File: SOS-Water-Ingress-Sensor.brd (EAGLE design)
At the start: 160 x 100 mm, 1 part

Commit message: Update board design and schematic.
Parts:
- added JP1: (no value), SparkFun-Connectors:1X03
- added Q1: (no value), SparkFun-DiscreteSemi:SOT23-3
- added R1, R3: 10K, resistor:R0603
- added R2: 200K, resistor:R0603
- added U$1, U$2, U$3, U$4: JSH-GH-2VERT, BlueRobotics-JST-GH:JST-GH-TOP-2
- added U$5: JST-GH-3VERT, BlueRobotics-JST-GH:JST-GH-TOP-3
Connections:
- new net GND: JP1.1, R3.2, U$1.2, U$2.2, U$3.2, U$4.2
- new net N$1: Q1.1, R1.1, R2.1
- new net PROBE: R1.2, U$1.1, U$2.1, U$3.1, U$4.1
- new net SIGNAL: JP1.3, Q1.3, R3.1
- new net VCC: JP1.2, Q1.2, R2.2
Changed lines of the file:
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@@
 <elements>
 <element name="U$7" library="BR-Eagle-Library" package="BR-LOGO-SMALL" value="LOGOBR-LOGO-S" x="-15.24" y="1.27"/>
+<element name="JP1" library="SparkFun-Connectors" package="1X03" value="" x="-13.97" y="-7.62"/>
+<element name="R2" library="resistor" package="R0603" value="200K" x="-13.97" y="-11.43"/>
+<element name="R1" library="resistor" package="R0603" value="10K" x="-19.05" y="-15.24"/>
+<element name="U$1" library="BlueRobotics-JST-GH" package="JST-GH-TOP-2" value="JSH-GH-2VERT" x="-17.78" y="-26.67"/>
+<element name="Q1" library="SparkFun-DiscreteSemi" package="SOT23-3" value="" x="-22.86" y="-29.21"/>
+<element name="R3" library="resistor" package="R0603" value="10K" x="-22.86" y="-33.02"/>
+<element name="U$2" library="BlueRobotics-JST-GH" package="JST-GH-TOP-2" value="JSH-GH-2VERT" x="-21.59" y="-36.83"/>
+<element name="U$3" library="BlueRobotics-JST-GH" package="JST-GH-TOP-2" value="JSH-GH-2VERT" x="-21.59" y="-43.18"/>
+<element name="U$4" library="BlueRobotics-JST-GH" package="JST-GH-TOP-2" value="JSH-GH-2VERT" x="-21.59" y="-49.53"/>
+<element name="U$5" library="BlueRobotics-JST-GH" package="JST-GH-TOP-3" value="JST-GH-3VERT" x="-21.59" y="-55.88"/>
 </elements>
 <signals>
+<signal name="VCC">
+<contactref element="R2" pad="2"/>
+<contactref element="Q1" pad="2"/>
+<contactref element="JP1" pad="2"/>
+<wire x1="-13.12" y1="-11.43" x2="-21.91" y2="-30.21" width="0" layer="19" extent="1-1"/>
+<wire x1="-11.43" y1="-7.62" x2="-13.12" y2="-11.43" width="0" layer="19" extent="1-1"/>
+</signal>
+<signal name="GND">
+<contactref element="JP1" pad="1"/>
+<contactref element="U$1" pad="2"/>
+<contactref element="R3" pad="2"/>
+<contactref element="U$4" pad="2"/>
+<contactref element="U$2" pad="2"/>
+<contactref element="U$3" pad="2"/>
+<wire x1="-21.59" y1="-43.18" x2="-21.59" y2="-49.53" width="0" layer="19" extent="1-1"/>
+<wire x1="-21.59" y1="-36.83" x2="-21.59" y2="-43.18" width="0" layer="19" extent="1-1"/>
+<wire x1="-22.01" y1="-33.02" x2="-21.59" y2="-36.83" width="0" layer="19" extent="1-1"/>
+<wire x1="-17.78" y1="-26.67" x2="-22.01" y2="-33.02" width="0" layer="19" extent="1-1"/>
+<wire x1="-13.97" y1="-7.62" x2="-17.78" y2="-26.67" width="0" layer="19" extent="1-1"/>
+</signal>
+<signal name="SIGNAL">
+<contactref element="JP1" pad="3"/>
+<contactref element="Q1" pad="3"/>
+<contactref element="R3" pad="1"/>
+<wire x1="-22.86" y1="-28.11" x2="-23.71" y2="-33.02" width="0" layer="19" extent="1-1"/>
+<wire x1="-8.89" y1="-7.62" x2="-22.86" y2="-28.11" width="0" layer="19" extent="1-1"/>
+</signal>
+<signal name="N$1">
+<contactref element="R1" pad="1"/>
+<contactref element="Q1" pad="1"/>
+<contactref element="R2" pad="1"/>
+<wire x1="-19.9" y1="-15.24" x2="-23.81" y2="-30.21" width="0" layer="19" extent="1-1"/>
+<wire x1="-14.82" y1="-11.43" x2="-19.9" y2="-15.24" width="0" layer="19" extent="1-1"/>
+</signal>
+<signal name="PROBE">
+<contactref element="U$1" pad="1"/>
+<contactref element="R1" pad="2"/>
+<contactref element="U$4" pad="1"/>
+<contactref element="U$2" pad="1"/>
+<contactref element="U$3" pad="1"/>
+<wire x1="-20.34" y1="-43.18" x2="-20.34" y2="-49.53" width="0" layer="19" extent="1-1"/>
+<wire x1="-20.34" y1="-36.83" x2="-20.34" y2="-43.18" width="0" layer="19" extent="1-1"/>
+<wire x1="-16.53" y1="-26.67" x2="-20.34" y2="-36.83" width="0" layer="19" extent="1-1"/>
+<wire x1="-18.2" y1="-15.24" x2="-16.53" y2="-26.67" width="0" layer="19" extent="1-1"/>
+</signal>
 </signals>
 </board>

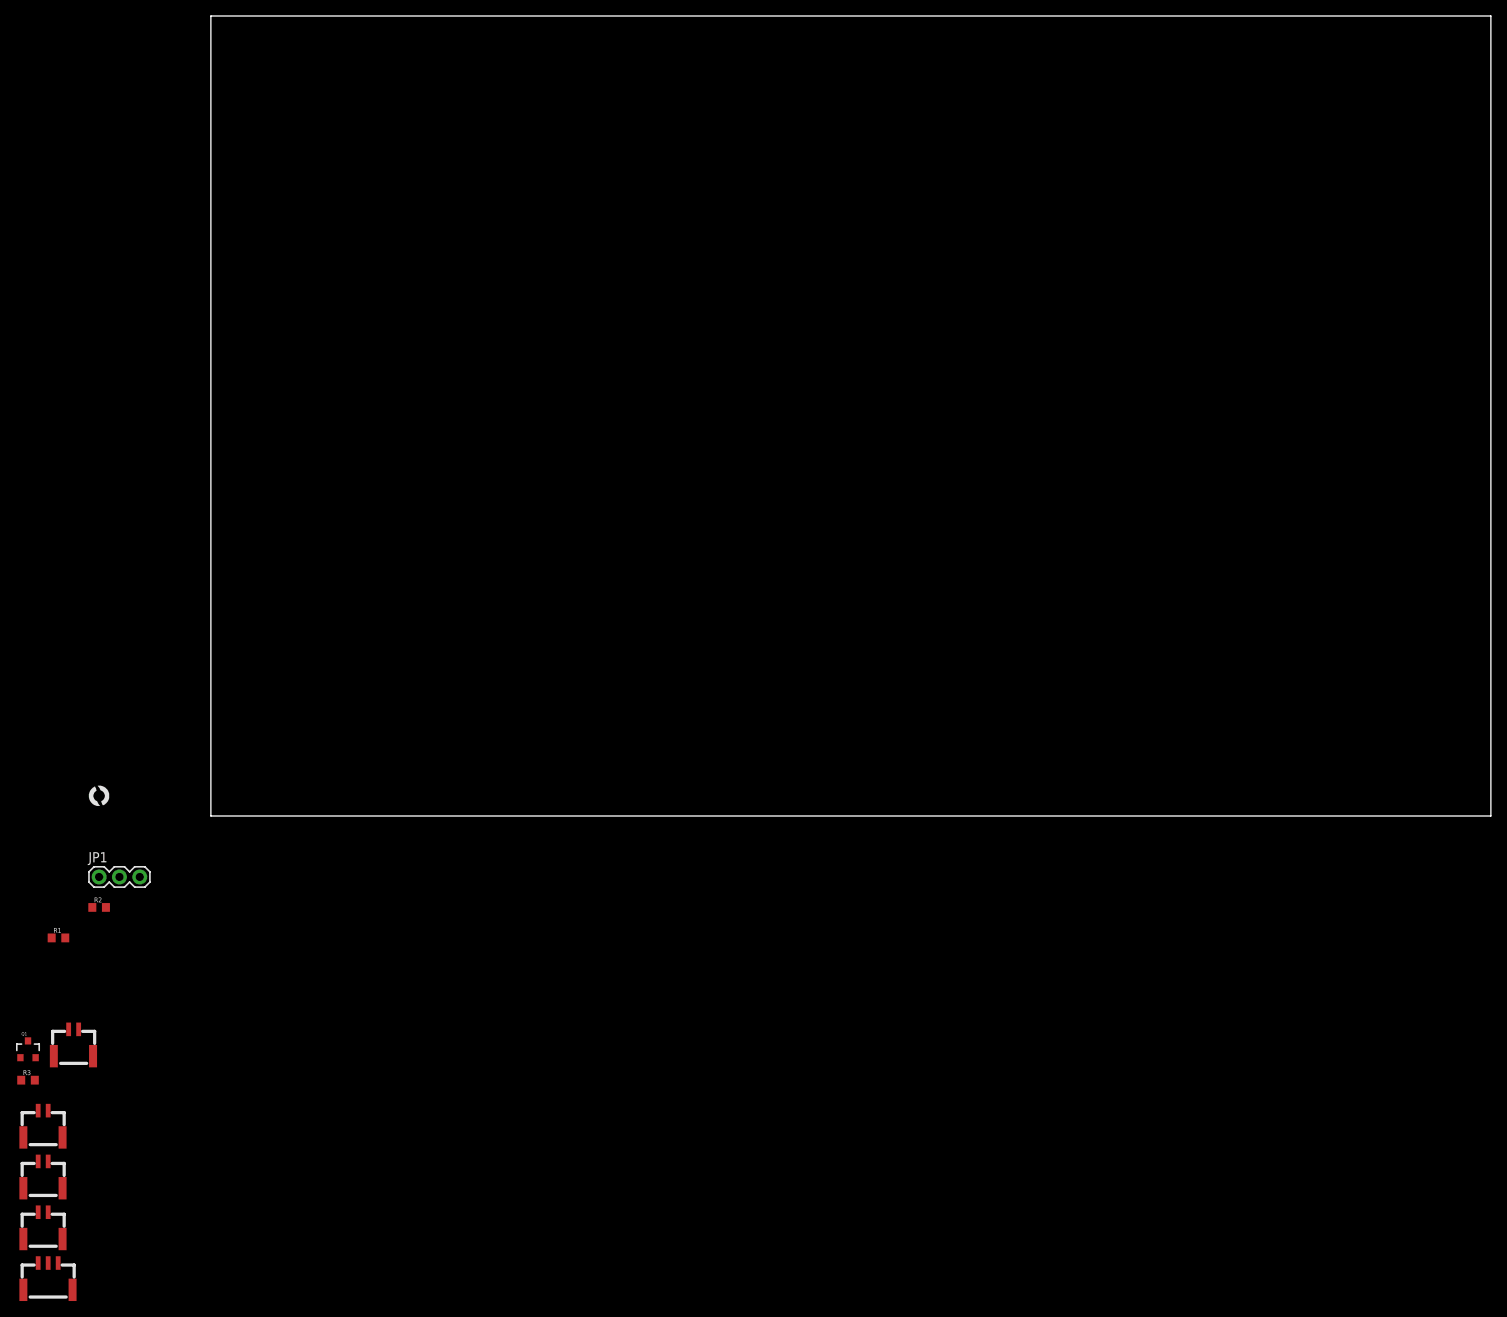
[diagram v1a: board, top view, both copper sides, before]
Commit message: Added LED indicator and resistor, completed board layout.
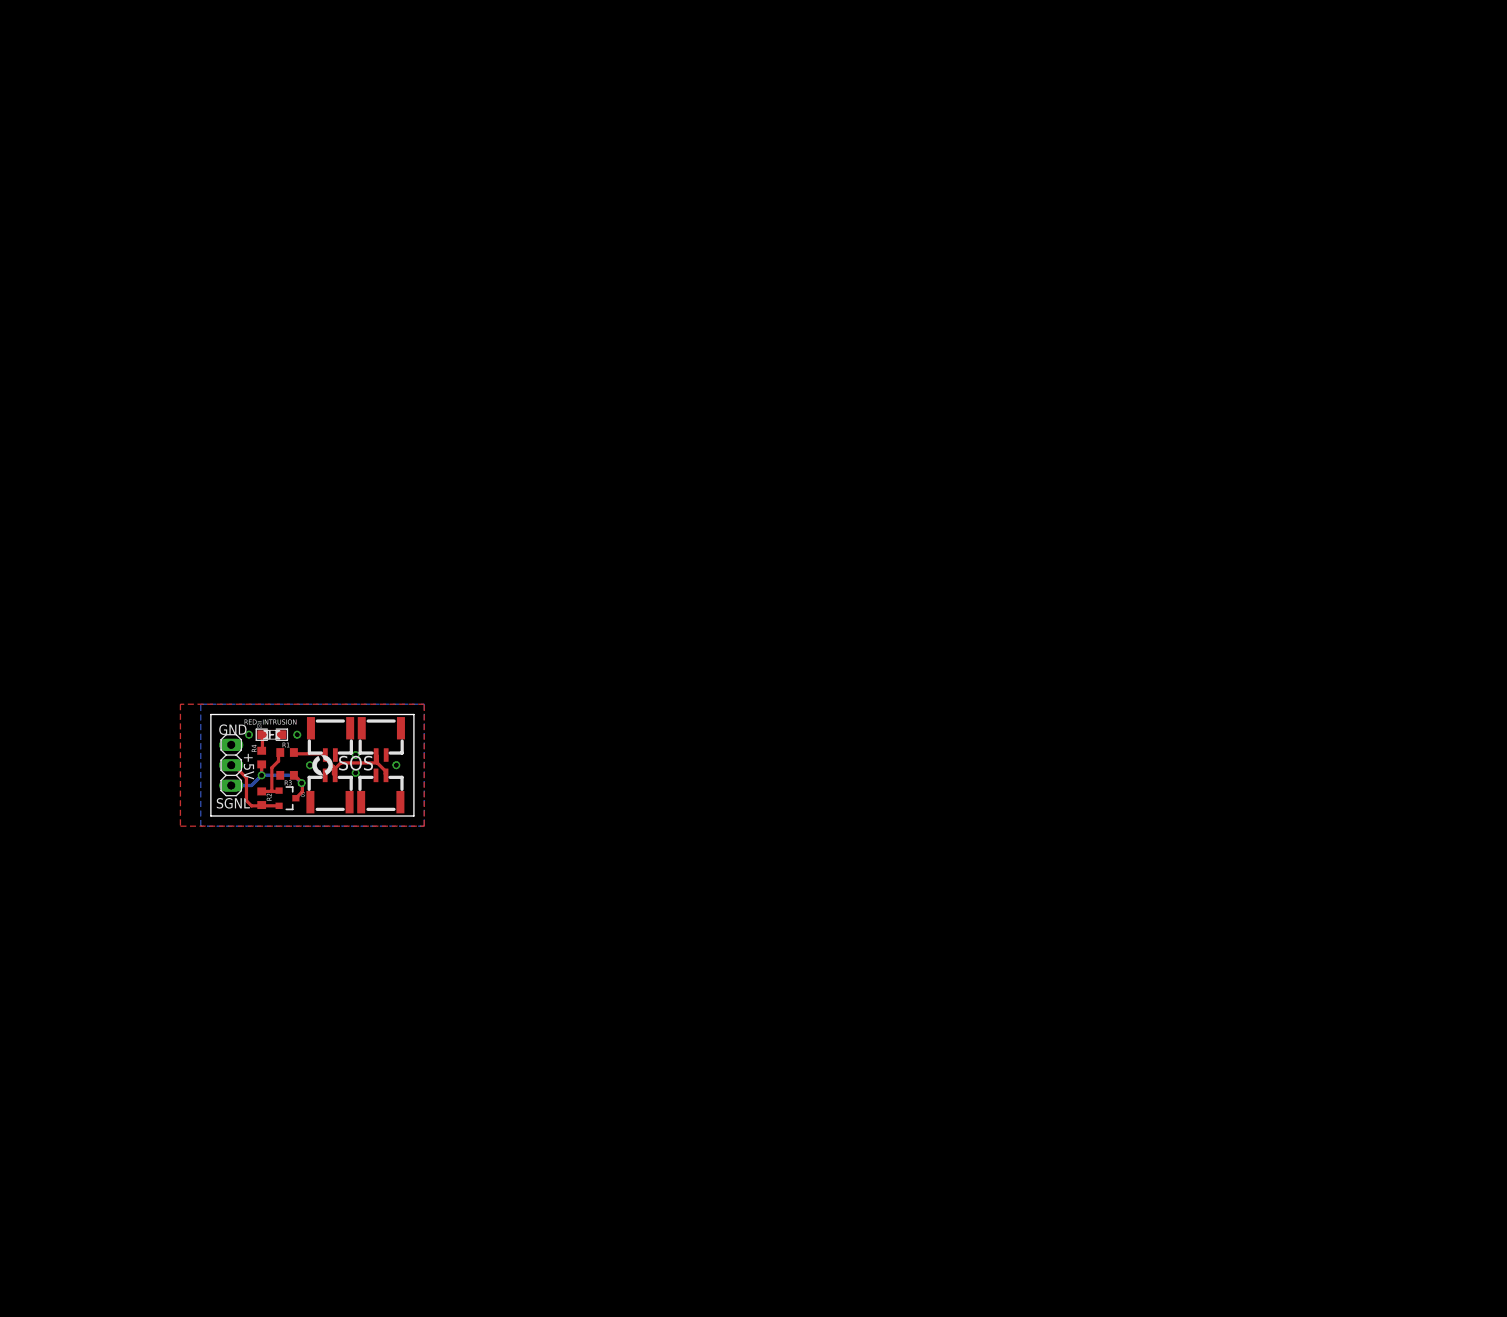
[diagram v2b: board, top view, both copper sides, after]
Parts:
- removed U$5: JST-GH-3VERT, BlueRobotics-JST-GH:JST-GH-TOP-3
- added D1: (no value), standardparts:0805.LED
- added R4: 250, resistor:R0603
- JP1: device SparkFun-Connectors:1X03 -> pinhead+:1X03
- R2: value 200K -> 12K
- moved U$4 71.8 mm to (21.9, 7.62), turned to 180 degrees
- moved U$3 62.9 mm to (15.6, 7.62), turned to 180 degrees
- moved U$2 59.5 mm to (20.6, 5.08)
- moved R3 50.0 mm to (9.53, 5.08), turned to 180 degrees
- moved Q1 45.1 mm to (9.53, 2.22), turned to 270 degrees
- moved U$1 45.1 mm to (14.3, 5.08)
- moved R1 36.8 mm to (9.53, 7.94)
- moved U$7 28.2 mm to (12.7, 5.08)
- moved R2 24.5 mm to (6.35, 2.22), turned to 270 degrees
- moved JP1 21.6 mm to (2.54, 6.35), turned to 270 degrees
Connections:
- new net N$2: D1.P$1, R4.2
- net GND: now also D1.P$2
- net SIGNAL: now also R4.1
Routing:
- net PROBE: track 0.00 -> 16.8 mm
- net SIGNAL: track 0.00 -> 14.9 mm, vias 0 -> 2
- net VCC: track 0.00 -> 9.85 mm
- net N$1: track 0.00 -> 7.54 mm
- net N$2: track 0.00 -> 2.05 mm
- added copper zone on layer 1, net GND
- added copper zone on layer 16, net GND
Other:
- board size 160 x 100 mm -> 25.4 x 12.7 mm
- board text added: "+5V"
- board text added: "A.S. 8/16"
- board text added: "BlueRobotics SOS Water Ingress Sensor"
- board text added: "GND"
- board text added: "RED=INTRUSION"
- board text added: "SGNL"
- board text added: "SOS"
- board text added: "rev1"

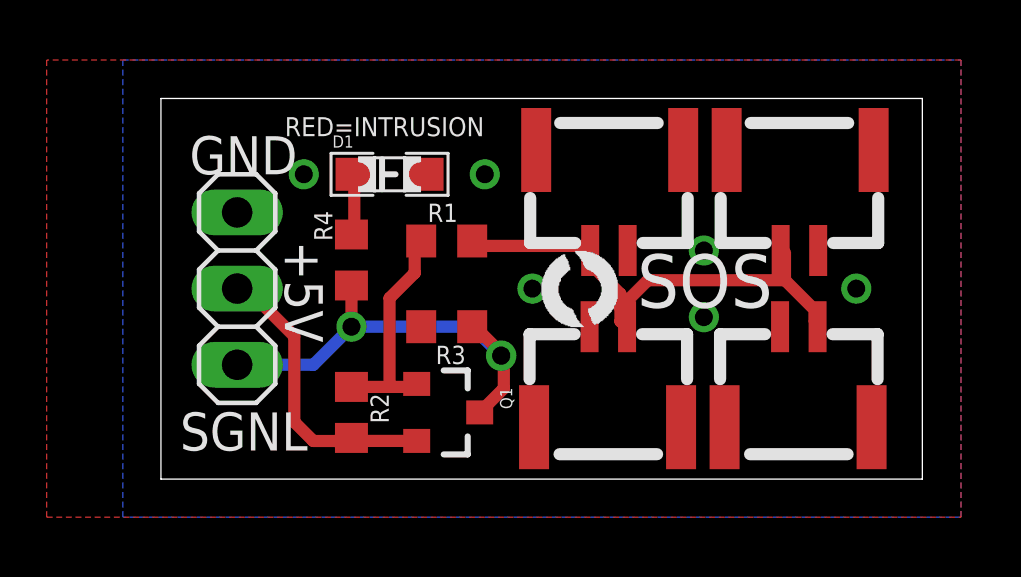
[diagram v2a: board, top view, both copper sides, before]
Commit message: Update silkscreen and layout.
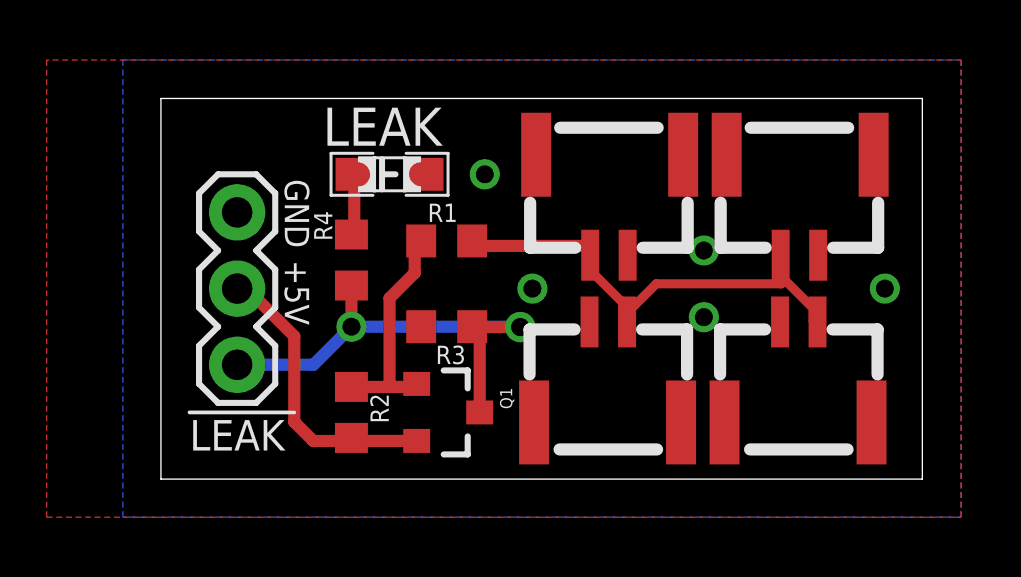
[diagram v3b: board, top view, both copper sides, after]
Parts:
- JP1: device pinhead+:1X03 -> SparkFun-Connectors:1X03
- R4: value 250 -> 240
- moved U$7 12.5 mm to (24.4, 0.95), flipped to the bottom
- moved JP1 2.54 mm to (2.54, 8.89)
- moved U$3 0.16 mm to (15.6, 7.46)
- moved U$4 0.16 mm to (21.9, 7.46)
- moved U$1 0.16 mm to (14.3, 5.24)
- moved U$2 0.16 mm to (20.6, 5.24)
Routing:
- net SIGNAL: track 14.9 -> 16.1 mm
- net PROBE: track 16.8 -> 16.1 mm
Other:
- board text added: "LEAK"
- board text added: "SOS Leak Sensor Probe Host Board"
- board text removed: "BlueRobotics SOS Water Ingress Sensor"
- board text removed: "RED=INTRUSION"
- board text removed: "SGNL"
- board text removed: "SOS"

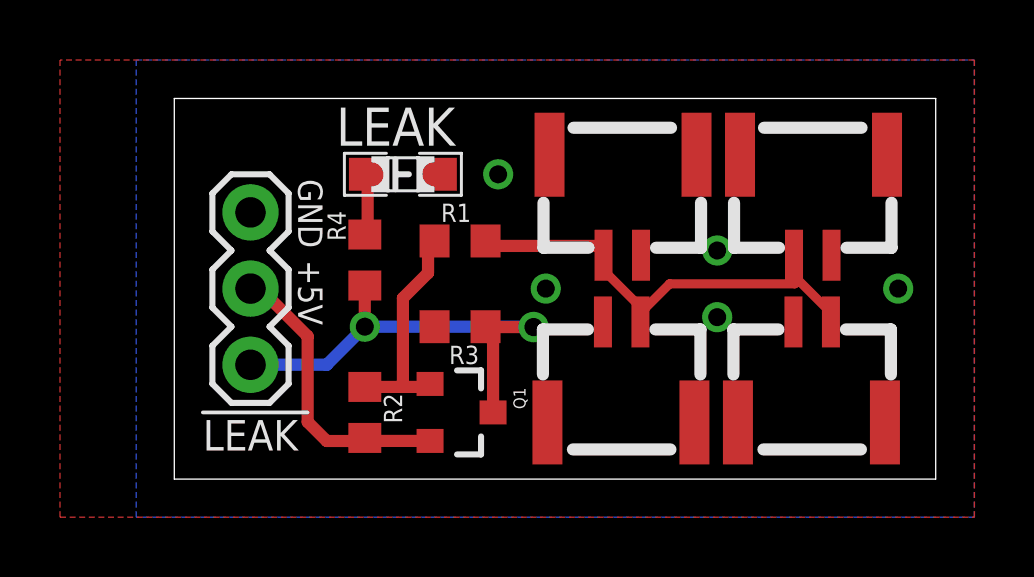
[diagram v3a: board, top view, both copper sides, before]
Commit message: Widened board slightly and fixed all clearance errors.
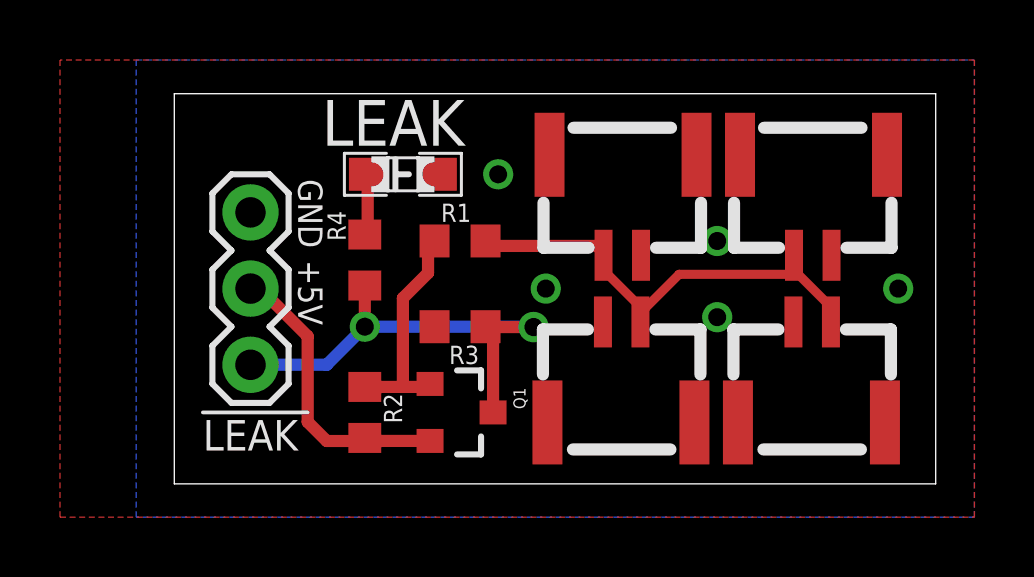
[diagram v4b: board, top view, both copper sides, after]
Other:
- board size 25.4 x 12.7 mm -> 25.4 x 13 mm
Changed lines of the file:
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@@
 <?xml version="1.0" encoding="utf-8"?>
 <!DOCTYPE eagle SYSTEM "eagle.dtd">
-<eagle version="7.4.0">
+<eagle version="7.6.0">
 <drawing>
 <settings>
@@
 <board>
 <plain>
-<wire x1="0" y1="0" x2="25.38" y2="0" width="0" layer="20"/>
-<wire x1="25.38" y1="0" x2="25.38" y2="12.6875" width="0" layer="20"/>
-<wire x1="25.38" y1="12.6875" x2="0" y2="12.6875" width="0" layer="20"/>
-<wire x1="0" y1="12.6875" x2="0" y2="0" width="0" layer="20"/>
-<text x="5.3975" y="11.1125" size="1.27" layer="25" ratio="12">LEAK</text>
+<wire x1="0" y1="-0.15875" x2="25.38" y2="-0.15875" width="0" layer="20"/>
+<wire x1="25.38" y1="-0.15875" x2="25.38" y2="12.84625" width="0" layer="20"/>
+<wire x1="25.38" y1="12.84625" x2="0" y2="12.84625" width="0" layer="20"/>
+<wire x1="0" y1="12.84625" x2="0" y2="-0.15875" width="0" layer="20"/>
+<text x="4.92125" y="11.1125" size="1.524" layer="25" ratio="12">LEAK</text>
 <text x="14.9225" y="3.81" size="0.635" layer="26" ratio="12" rot="MR0">rev1</text>
 <text x="16.1925" y="0.635" size="0.635" layer="26" ratio="12" rot="MR0">A.S. 8/16</text>
@@
 <via x="10.795" y="10.16" extent="1-16" drill="0.6"/>
 <via x="12.3825" y="6.35" extent="1-16" drill="0.6"/>
-<via x="18.0975" y="7.62" extent="1-16" drill="0.6"/>
+<via x="18.0975" y="7.9375" extent="1-16" drill="0.6"/>
 <via x="18.0975" y="5.3975" extent="1-16" drill="0.6"/>
 <via x="24.13" y="6.35" extent="1-16" drill="0.6"/>
@@
 <contactref element="U$3" pad="1"/>
 <contactref element="U$4" pad="1"/>
-<wire x1="20.64385" y1="6.6294" x2="20.64385" y2="7.5438" width="0.4064" layer="1"/>
 <wire x1="21.717" y1="5.2578" x2="21.717" y2="5.715" width="0.254" layer="1"/>
 <wire x1="20.64385" y1="7.5438" x2="20.6575" y2="7.46125" width="0.254" layer="1"/>
@@
 <wire x1="15.5575" y1="5.1" x2="15.5375" y2="5.23875" width="0.3048" layer="1"/>
 <wire x1="15.5575" y1="5.715" x2="15.71625" y2="5.715" width="0.3048" layer="1"/>
-<wire x1="15.71625" y1="5.715" x2="16.51" y2="6.50875" width="0.3048" layer="1"/>
-<wire x1="16.51" y1="6.50875" x2="20.68195" y2="6.50875" width="0.3048" layer="1"/>
-<wire x1="20.68195" y1="6.50875" x2="20.64385" y2="6.6294" width="0.3048" layer="1"/>
-<wire x1="20.64385" y1="6.6294" x2="20.8026" y2="6.6294" width="0.3048" layer="1"/>
-<wire x1="20.8026" y1="6.6294" x2="21.717" y2="5.715" width="0.3048" layer="1"/>
+<wire x1="20.79625" y1="6.82625" x2="21.8875" y2="5.735" width="0.3048" layer="1"/>
+<wire x1="21.8875" y1="5.735" x2="21.8875" y2="5.23875" width="0.3048" layer="1"/>
+<wire x1="20.6575" y1="7.46125" x2="20.79625" y2="7.3225" width="0.3048" layer="1"/>
+<wire x1="20.79625" y1="7.3225" x2="20.79625" y2="6.82625" width="0.3048" layer="1"/>
+<wire x1="20.79625" y1="6.82625" x2="16.8275" y2="6.82625" width="0.3048" layer="1"/>
+<wire x1="16.8275" y1="6.82625" x2="15.71625" y2="5.715" width="0.3048" layer="1"/>
 </signal>
 <signal name="N$2">
